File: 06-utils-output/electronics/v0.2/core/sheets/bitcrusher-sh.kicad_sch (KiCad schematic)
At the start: 22 parts, among them Q2 2N3819, U1 TL072, U2 TL072

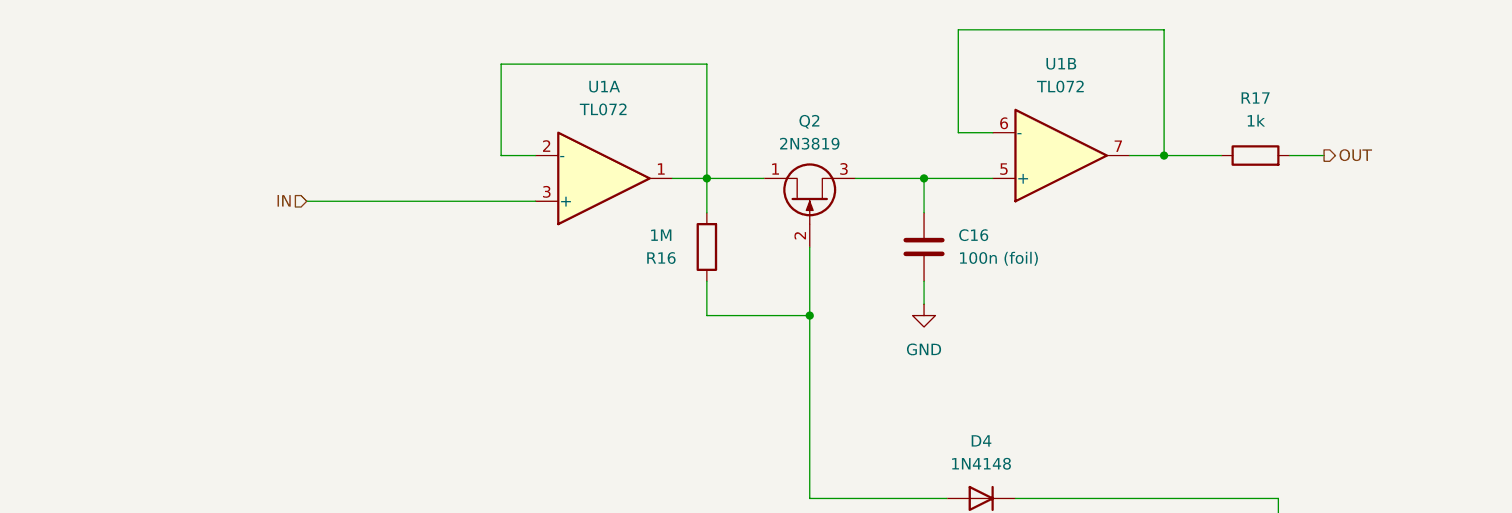
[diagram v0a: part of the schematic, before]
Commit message: Added protection diodes to utils + output
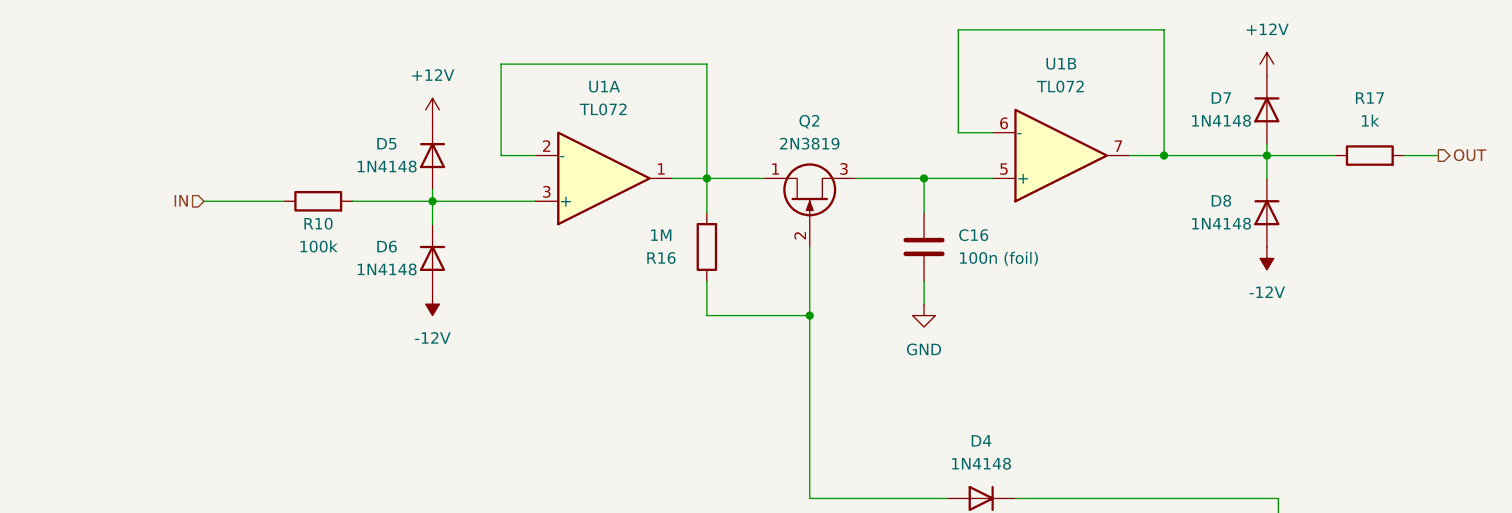
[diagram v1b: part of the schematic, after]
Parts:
- added D5, D6, D7, D8: 1N4148, Diode_SMD:D_SOD-123, symbol Device:D
- added R10: 100k, Resistor_SMD:R_0603_1608Metric, symbol Device:R
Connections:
- net +12V: now also D5.1 (K), D7.1 (K)
- net -12V: now also D6.2 (A), D8.2 (A)
- net IN: now also R10.1; no longer U1.3 (+)
- net at R17.1, U1.6 (-), U1.7: now also D7.2 (A), D8.1 (K)
- new net: D5.2 (A), D6.1 (K), R10.2, U1.3 (+)
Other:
- moved on the sheet: R17

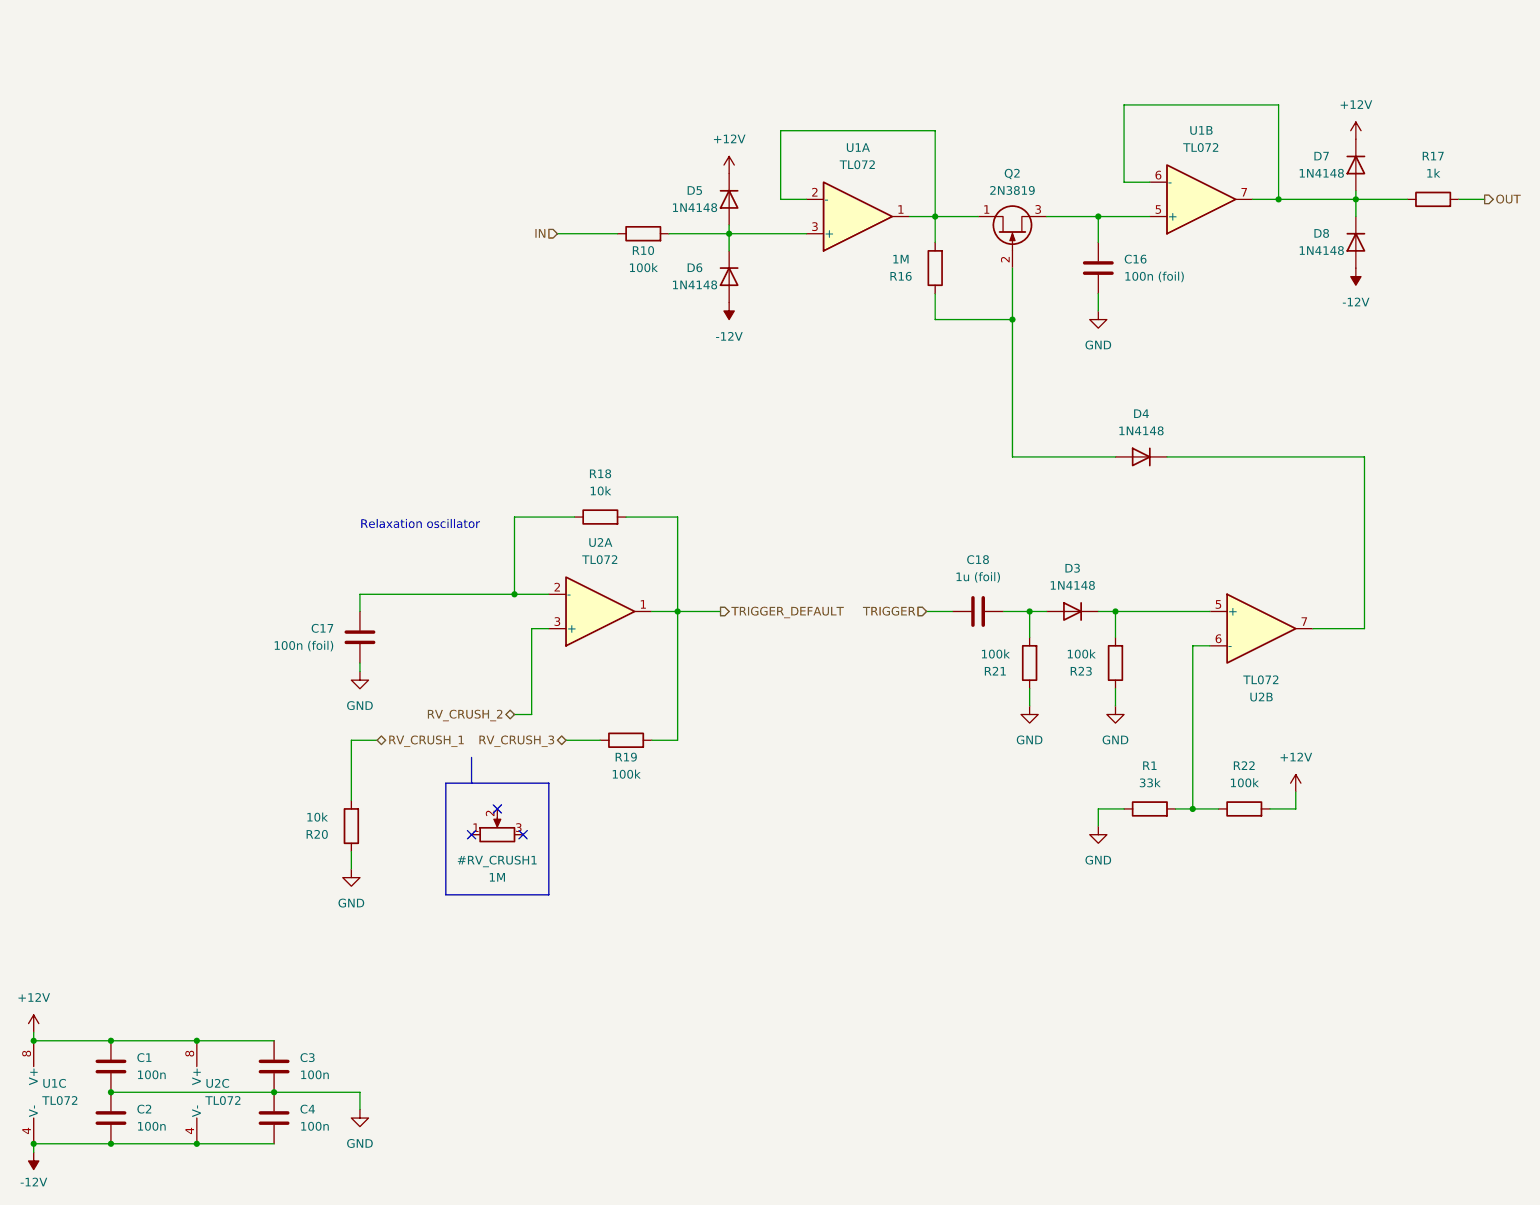
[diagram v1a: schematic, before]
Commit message: Bitcrusher tested and  refined
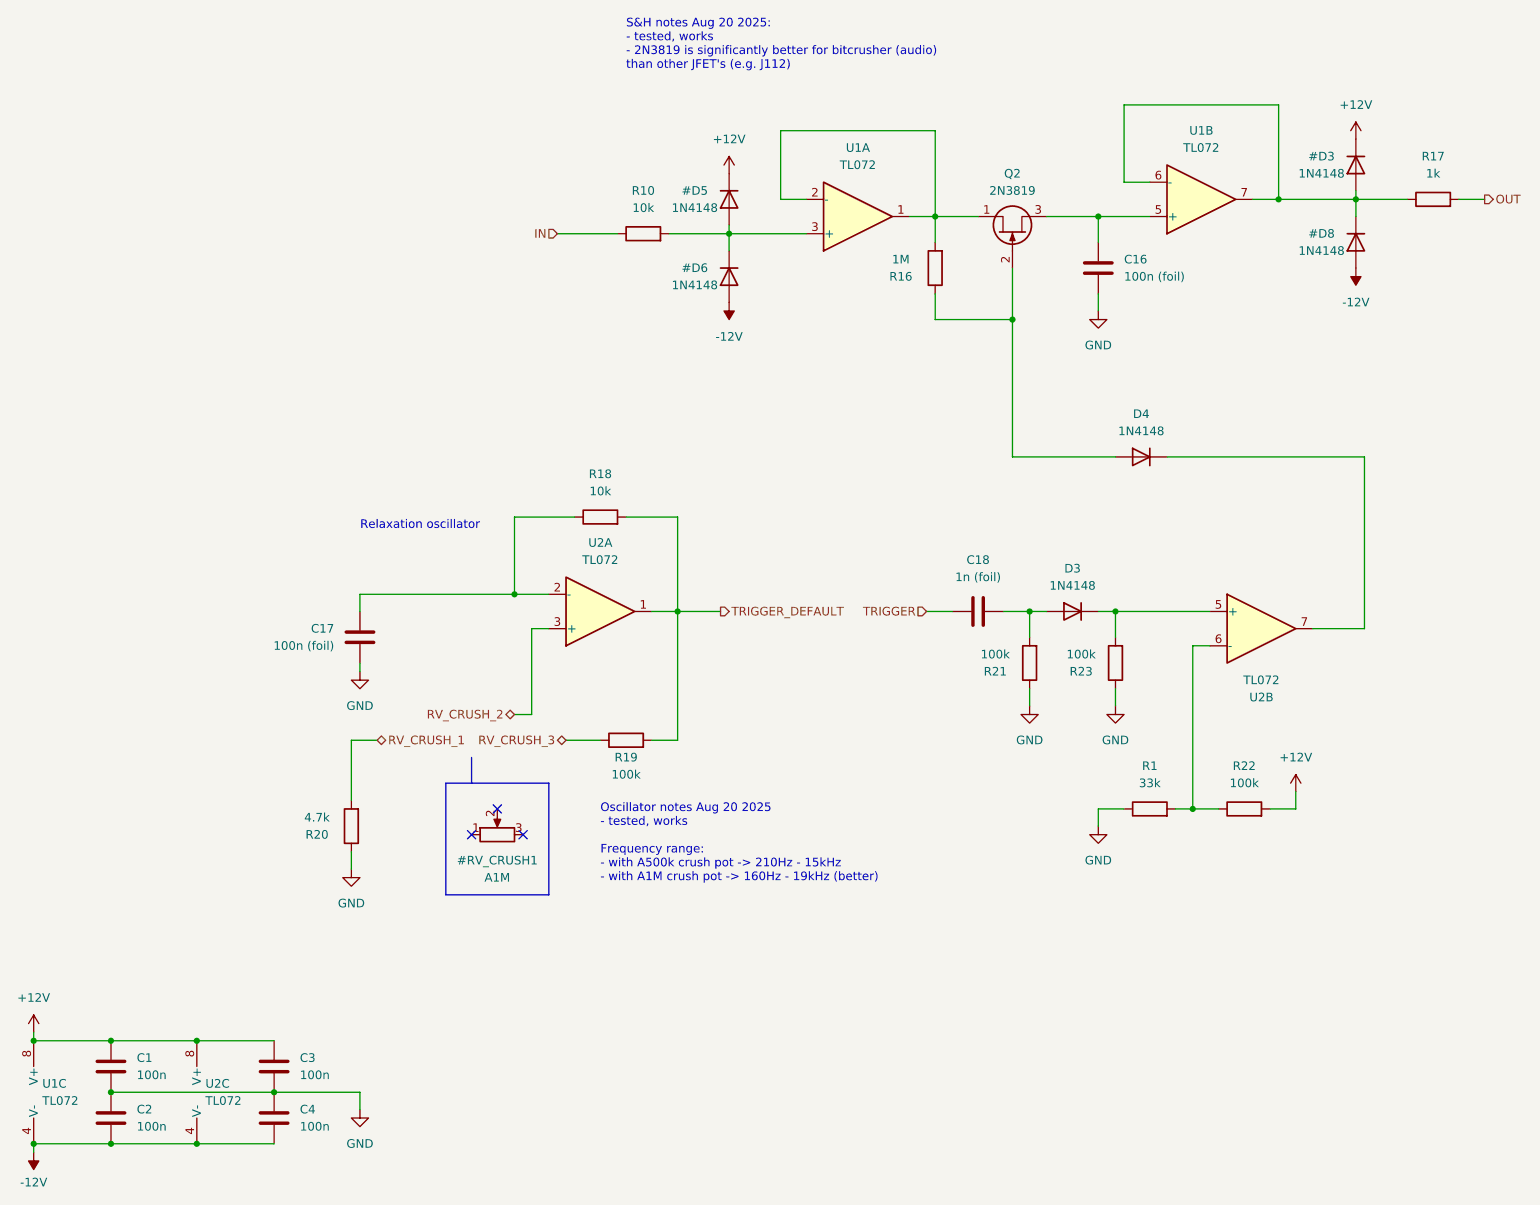
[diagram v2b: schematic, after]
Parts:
- #RV_CRUSH1: value 1M -> A1M
- C18: value 1u (foil) -> 1n (foil); footprint Capacitor_THT:C_Rect_L7.0mm_W4.5mm_P5.00mm -> Capacitor_THT:C_Rect_L7.2mm_W2.5mm_P5.00mm_FKS2_FKP2_MKS2_MKP2
- R10: value 100k -> 10k; LCSC C25803 -> C25804
- R20: value 10k -> 4.7k
- renumbered D7 to #D3, D5 to #D5, D6 to #D6, D8 to #D8
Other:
- note added: "Oscillator notes Aug 20 2025 - tested, works Frequency range: - with A500k crush pot -> 210Hz - 15kHz - with A1M crush pot -> 160Hz - 19kHz (better)"
- note added: "S&H notes Aug 20 2025: - tested, works - 2N3819 is significantly better for bitcrusher (audio) than other JFET's (e.g. J112)"
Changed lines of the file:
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@@
 		)
 	)
+	(text "S&H notes Aug 20 2025:\n- tested, works\n- 2N3819 is significantly better for bitcrusher (audio)\nthan other JFET's (e.g. J112)"
+		(exclude_from_sim no)
+		(at 109.22 22.86 0)
+		(effects
+			(font
+				(size 1.27 1.27)
+				(thickness 0.1588)
+				(color 0 194 194 1)
+			)
+			(justify left)
+		)
+	)
+	(text "Oscillator notes Aug 20 2025\n- tested, works\n\nFrequency range:\n- with A500k crush pot -> 210Hz - 15kHz\n- with A1M crush pot -> 160Hz - 19kHz (better)"
+		(exclude_from_sim no)
+		(at 105.41 140.97 0)
+		(effects
+			(font
+				(size 1.27 1.27)
+				(thickness 0.1588)
+				(color 0 194 194 1)
+			)
+			(justify left)
+		)
+	)
 	(junction
 		(at 179.07 48.26)
@@
 	)
 	(symbol
+		(lib_id "Device:R")
+		(at 111.76 50.8 90)
+		(unit 1)
+		(exclude_from_sim no)
+		(in_bom yes)
+		(on_board yes)
+		(dnp no)
+		(property "Reference" "R10"
+			(at 111.76 44.45 90)
+			(effects
+				(font
+					(size 1.27 1.27)
+				)
+			)
+		)
+		(property "Value" "10k"
+			(at 111.76 46.99 90)
+			(effects
+				(font
+					(size 1.27 1.27)
+				)
+			)
+		)
+		(property "Footprint" "Resistor_SMD:R_0603_1608Metric"
+			(at 111.76 52.578 90)
+			(effects
+				(font
+					(size 1.27 1.27)
+				)
+				(hide yes)
+			)
+		)
+		(property "Datasheet" "~"
+			(at 111.76 50.8 0)
+			(effects
+				(font
+					(size 1.27 1.27)
+				)
+				(hide yes)
+			)
+		)
+		(property "Description" ""
+			(at 111.76 50.8 0)
+			(effects
+				(font
+					(size 1.27 1.27)
+				)
+				(hide yes)
+			)
+		)
+		(property "LCSC" "C25804"
+			(at 111.76 50.8 90)
+			(effects
+				(font
+					(size 1.27 1.27)
+				)
+				(hide yes)
+			)
+		)
+		(property "Mouser" ""
+			(at 111.76 50.8 0)
+			(effects
+				(font
+					(size 1.27 1.27)
+				)
+				(hide yes)
+			)
+		)
+		(property "Part No." ""
+			(at 111.76 50.8 0)
+			(effects
+				(font
+					(size 1.27 1.27)
+				)
+				(hide yes)
+			)
+		)
+		(property "Part URL" ""
+			(at 111.76 50.8 0)
+			(effects
+				(font
+					(size 1.27 1.27)
+				)
+				(hide yes)
+			)
+		)
+		(property "Vendor" "JLCPCB"
+			(at 111.76 50.8 0)
+			(effects
+				(font
+					(size 1.27 1.27)
+				)
+				(hide yes)
+			)
+		)
+		(property "Field4" ""
+			(at 111.76 50.8 0)
+			(effects
+				(font
+					(size 1.27 1.27)
+				)
+				(hide yes)
+			)
+		)
+		(pin "1"
+		)
+		(pin "2"
+		)
+		(instances
+			(project "utils-output-core"
+				(path "/8e2e31f3-eed5-4de1-966c-f4162758c735/db8ca729-d0ac-4a4b-85bc-9e88a5b3d47c"
+					(reference "R10")
+					(unit 1)
+				)
+			)
+		)
+	)
+	(symbol
 		(lib_id "power:GND")
 		(at 179.07 62.23 0)
@@
 		(on_board yes)
 		(dnp no)
-		(property "Reference" "D6"
+		(property "Reference" "#D6"
 			(at 119.38 55.88 90)
 			(effects
@@
 			(project "utils-output-core"
 				(path "/8e2e31f3-eed5-4de1-966c-f4162758c735/db8ca729-d0ac-4a4b-85bc-9e88a5b3d47c"
-					(reference "D6")
+					(reference "#D6")
 					(unit 1)
 				)
@@
 		(on_board yes)
 		(dnp no)
-		(property "Reference" "D5"
+		(property "Reference" "#D5"
 			(at 119.38 44.45 90)
 			(effects
@@
 			(project "utils-output-core"
 				(path "/8e2e31f3-eed5-4de1-966c-f4162758c735/db8ca729-d0ac-4a4b-85bc-9e88a5b3d47c"
-					(reference "D5")
+					(reference "#D5")
 					(unit 1)
 				)
@@
 	)
 	(symbol
-		(lib_id "Device:R")
-		(at 111.76 50.8 90)
-		(unit 1)
-		(exclude_from_sim no)
-		(in_bom yes)
-		(on_board yes)
-		(dnp no)
-		(property "Reference" "R10"
-			(at 111.76 53.34 90)
-			(effects
-				(font
-					(size 1.27 1.27)
-				)
-			)
-		)
-		(property "Value" "100k"
-			(at 111.76 55.88 90)
-			(effects
-				(font
-					(size 1.27 1.27)
-				)
-			)
-		)
-		(property "Footprint" "Resistor_SMD:R_0603_1608Metric"
-			(at 111.76 52.578 90)
-			(effects
-				(font
-					(size 1.27 1.27)
-				)
-				(hide yes)
-			)
-		)
-		(property "Datasheet" "~"
-			(at 111.76 50.8 0)
-			(effects
-				(font
-					(size 1.27 1.27)
-				)
-				(hide yes)
-			)
-		)
-		(property "Description" ""
-			(at 111.76 50.8 0)
-			(effects
-				(font
-					(size 1.27 1.27)
-				)
-				(hide yes)
-			)
-		)
-		(property "LCSC" "C25803"
-			(at 111.76 50.8 90)
-			(effects
-				(font
-					(size 1.27 1.27)
-				)
-				(hide yes)
-			)
-		)
-		(property "Mouser" ""
-			(at 111.76 50.8 0)
-			(effects
-				(font
-					(size 1.27 1.27)
-				)
-				(hide yes)
-			)
-		)
-		(property "Part No." ""
-			(at 111.76 50.8 0)
-			(effects
-				(font
-					(size 1.27 1.27)
-				)
-				(hide yes)
-			)
-		)
-		(property "Part URL" ""
-			(at 111.76 50.8 0)
-			(effects
-				(font
-					(size 1.27 1.27)
-				)
-				(hide yes)
-			)
-		)
-		(property "Vendor" "JLCPCB"
-			(at 111.76 50.8 0)
-			(effects
-				(font
-					(size 1.27 1.27)
-				)
-				(hide yes)
-			)
-		)
-		(property "Field4" ""
-			(at 111.76 50.8 0)
-			(effects
-				(font
-					(size 1.27 1.27)
-				)
-				(hide yes)
-			)
-		)
-		(pin "1"
-		)
-		(pin "2"
-		)
-		(instances
-			(project "utils-output-core"
-				(path "/8e2e31f3-eed5-4de1-966c-f4162758c735/db8ca729-d0ac-4a4b-85bc-9e88a5b3d47c"
-					(reference "R10")
-					(unit 1)
-				)
-			)
-		)
-	)
-	(symbol
 		(lib_id "power:GND")
 		(at 69.85 115.57 0)
@@
 		(on_board yes)
 		(dnp no)
-		(property "Reference" "D7"
+		(property "Reference" "#D3"
 			(at 212.09 39.37 90)
 			(effects
@@
 			(project "utils-output-core"
 				(path "/8e2e31f3-eed5-4de1-966c-f4162758c735/db8ca729-d0ac-4a4b-85bc-9e88a5b3d47c"
-					(reference "D7")
+					(reference "#D3")
 					(unit 1)
 				)
@@
 		(on_board yes)
 		(dnp no)
-		(property "Reference" "D8"
+		(property "Reference" "#D8"
 			(at 212.09 50.8 90)
 			(effects
@@
 			(project "utils-output-core"
 				(path "/8e2e31f3-eed5-4de1-966c-f4162758c735/db8ca729-d0ac-4a4b-85bc-9e88a5b3d47c"
-					(reference "D8")
+					(reference "#D8")
 					(unit 1)
 				)
@@
 			)
 		)
-		(property "Value" "1M"
+		(property "Value" "A1M"
 			(at 90.17 146.05 90)
 			(effects
@@
 			)
 		)
-		(property "Value" "10k"
+		(property "Value" "4.7k"
 			(at 63.5 137.16 0)
 			(effects
@@
 			)
 		)
-		(property "Value" "1u (foil)"
+		(property "Value" "1n (foil)"
 			(at 161.29 101.6 90)
 			(effects
@@
 			)
 		)
-		(property "Footprint" "Capacitor_THT:C_Rect_L7.0mm_W4.5mm_P5.00mm"
+		(property "Footprint" "Capacitor_THT:C_Rect_L7.2mm_W2.5mm_P5.00mm_FKS2_FKP2_MKS2_MKP2"
 			(at 165.1 105.7148 0)
 			(effects
